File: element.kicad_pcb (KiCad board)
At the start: 4 copper layers, 65.4 x 44.9 mm, 11 parts, among them J1 BANK_A, J2 BANK_C, J3 BANK_B, J4 BANK_D

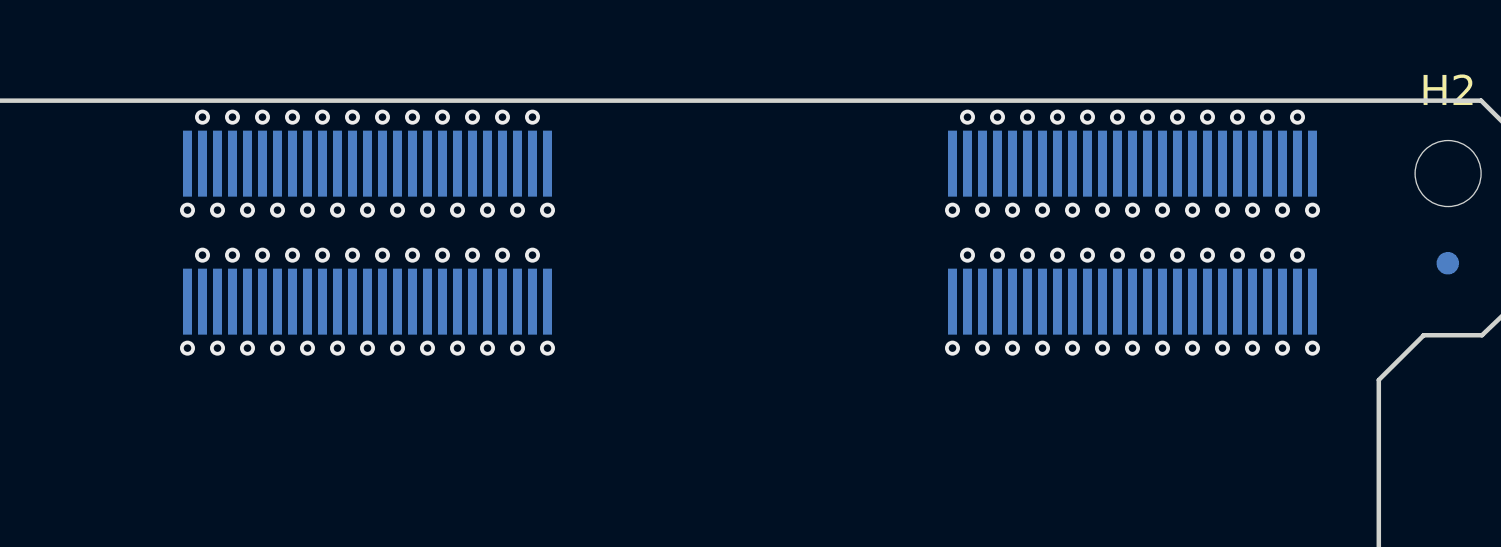
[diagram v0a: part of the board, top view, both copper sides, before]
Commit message: slight fix of port positions
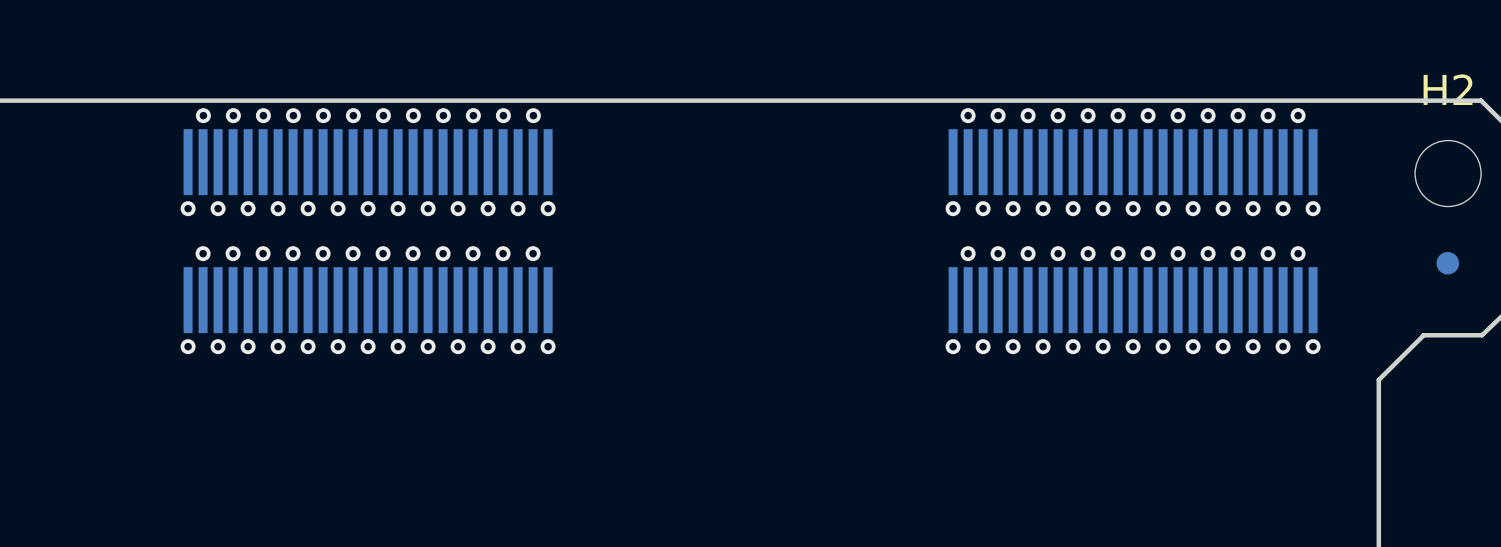
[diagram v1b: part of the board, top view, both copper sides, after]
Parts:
- moved J2 0.05 mm to (84.2, 49.7)
- moved J1 0.05 mm to (58.6, 49.7)
